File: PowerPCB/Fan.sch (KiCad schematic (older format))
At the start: 3 parts, among them Q2 Q_PMOS_DGS

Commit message: new relay added to PowerPCB, and its 3D model is added to the library
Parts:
- removed K?: FINDER-32.21-x300, Relay_THT:Relay_SPST_Finder_32.21-x300, symbol Relay:FINDER-32.21-x300
- added K3: ALFG2PF121, ALFG2PF121, symbol SamacSys_Parts:ALFG2PF121
- renumbered Q2 to Q1
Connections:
- wire segments 14 -> 15
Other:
- note added: "Relay: Panasonic ALFG2PF121 (Coil Voltage 12VDC, Coil Current 117mA, Contact Current Rating 31A)"
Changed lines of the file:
@@
 U 1 1 5E93960D
 P 1700 4450
-F 0 "R?" H 1770 4496 50  0000 L CNN
+F 0 "R8" H 1770 4496 50  0000 L CNN
 F 1 "100k" H 1770 4405 50  0000 L CNN
 F 2 "" V 1630 4450 50  0001 C CNN
@@
 VCC_12
 $Comp
-L Device:Q_PMOS_DGS Q2
+L Device:Q_PMOS_DGS Q1
 U 1 1 5EBA07C8
 P 3050 4650
-F 0 "Q?" H 3255 4696 50  0000 L CNN
+F 0 "Q1" H 3255 4696 50  0000 L CNN
 F 1 "Q_PMOS_DGS" H 3255 4605 50  0000 L CNN
 F 2 "" H 3250 4750 50  0001 C CNN
@@
 	3450 5150 3150 5150
 Wire Wire Line
-	4650 5000 4650 4850
-Wire Wire Line
-	5050 4950 5050 4850
+	6000 4500 5850 4500
 $Comp
-L power:GND #PWR?
+L power:GND #PWR01
 U 1 1 5EC359D9
-P 5050 4950
-F 0 "#PWR?" H 5050 4700 50  0001 C CNN
-F 1 "GND" H 5055 4777 50  0000 C CNN
-F 2 "" H 5050 4950 50  0001 C CNN
-F 3 "" H 5050 4950 50  0001 C CNN
-	1    5050 4950
+P 4450 4550
+F 0 "#PWR01" H 4450 4300 50  0001 C CNN
+F 1 "GND" H 4455 4377 50  0000 C CNN
+F 2 "" H 4450 4550 50  0001 C CNN
+F 3 "" H 4450 4550 50  0001 C CNN
+	1    4450 4550
+	1    0    0    -1
+$EndComp
+Text HLabel 4450 4400 0    50   Output ~ 0
+Fan-
+Text HLabel 6000 4500 2    50   Input ~ 0
+FanCtrl
+Text GLabel 6050 4400 2    50   Input ~ 0
+VCC_12
+Text Notes 5650 4950 0    50   ~ 0
+Relay: Panasonic ALFG2PF121 (Coil Voltage 12VDC, Coil Current 117mA, Contact Current Rating 31A)
+$Comp
+L SamacSys_Parts:ALFG2PF121 K3
+U 1 1 5ECACD05
+P 4650 4400
+F 0 "K3" H 5250 4665 50  0000 C CNN
+F 1 "ALFG2PF121" H 5250 4574 50  0000 C CNN
+F 2 "ALFG2PF121" H 5700 4500 50  0001 L CNN
+F 3 "http://www3.panasonic.biz/ac/e_download/control/relay/power/catalog/mech_eng_lfg.pdf" H 5700 4400 50  0001 L CNN
+F 4 "General Purpose Relays LF-G relay 1.8mm High cap type: 12V" H 5700 4300 50  0001 L CNN "Description"
+F 5 "23.3" H 5700 4200 50  0001 L CNN "Height"
+F 6 "Panasonic" H 5700 4100 50  0001 L CNN "Manufacturer_Name"
+F 7 "ALFG2PF121" H 5700 4000 50  0001 L CNN "Manufacturer_Part_Number"
+F 8 "769-ALFG2PF121" H 5700 3900 50  0001 L CNN "Mouser Part Number"
+F 9 "https://www.mouser.co.uk/ProductDetail/Panasonic-Industrial-Devices/ALFG2PF121?qs=WkdRfq4wf1O9EasQCWNl9Q%3D%3D" H 5700 3800 50  0001 L CNN "Mouser Price/Stock"
+F 10 "" H 5700 3700 50  0001 L CNN "RS Part Number"
+F 11 "" H 5700 3600 50  0001 L CNN "RS Price/Stock"
+	1    4650 4400
 	1    0    0    -1
 $EndComp
 Wire Wire Line
-	5150 4150 5150 4250
-$Comp
-L Relay:FINDER-32.21-x300 K?
-U 1 1 5EC302D7
-P 4850 4550
-F 0 "K?" H 5280 4596 50  0000 L CNN
-F 1 "FINDER-32.21-x300" H 5280 4505 50  0000 L CNN
-F 2 "Relay_THT:Relay_SPST_Finder_32.21-x300" H 6120 4520 50  0001 C CNN
-F 3 "http://gfinder.findernet.com/assets/Series/355/S32EN.pdf" H 4850 4550 50  0001 C CNN
-	1    4850 4550
-	1    0    0    -1
-$EndComp
-Text HLabel 5150 4150 1    50   Output ~ 0
-Fan-
-Text HLabel 4650 5000 3    50   Input ~ 0
-FanCtrl
-Text GLabel 4650 4150 1    50   Input ~ 0
-VCC_12
+	5850 4400 6050 4400
 Wire Wire Line
-	4650 4250 4650 4150
+	4450 4400 4650 4400
+Wire Wire Line
+	4650 4500 4450 4500
+Wire Wire Line
+	4450 4500 4450 4550
 $EndSCHEMATC

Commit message: Added footprints for all components
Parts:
- K3: footprint ALFG2PF121 -> SamacSys_Parts:ALFG2PF121
- Q1: footprint (none) -> Package_TO_SOT_SMD:SOT-323_SC-70_Handsoldering
- R8: footprint (none) -> Resistor_SMD:R_0805_2012Metric_Pad1.15x1.40mm_HandSolder
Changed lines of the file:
@@
 F 0 "R8" H 1770 4496 50  0000 L CNN
 F 1 "100k" H 1770 4405 50  0000 L CNN
-F 2 "" V 1630 4450 50  0001 C CNN
+F 2 "Resistor_SMD:R_0805_2012Metric_Pad1.15x1.40mm_HandSolder" V 1630 4450 50  0001 C CNN
 F 3 "~" H 1700 4450 50  0001 C CNN
 	1    1700 4450
@@
 F 0 "Q1" H 3255 4696 50  0000 L CNN
 F 1 "Q_PMOS_DGS" H 3255 4605 50  0000 L CNN
-F 2 "" H 3250 4750 50  0001 C CNN
+F 2 "Package_TO_SOT_SMD:SOT-323_SC-70_Handsoldering" H 3250 4750 50  0001 C CNN
 F 3 "~" H 3050 4650 50  0001 C CNN
 F 4 "X" H 3050 4650 50  0001 C CNN "Spice_Primitive"
@@
 F 0 "K3" H 5250 4665 50  0000 C CNN
 F 1 "ALFG2PF121" H 5250 4574 50  0000 C CNN
-F 2 "ALFG2PF121" H 5700 4500 50  0001 L CNN
+F 2 "SamacSys_Parts:ALFG2PF121" H 5700 4500 50  0001 L CNN
 F 3 "http://www3.panasonic.biz/ac/e_download/control/relay/power/catalog/mech_eng_lfg.pdf" H 5700 4400 50  0001 L CNN
 F 4 "General Purpose Relays LF-G relay 1.8mm High cap type: 12V" H 5700 4300 50  0001 L CNN "Description"

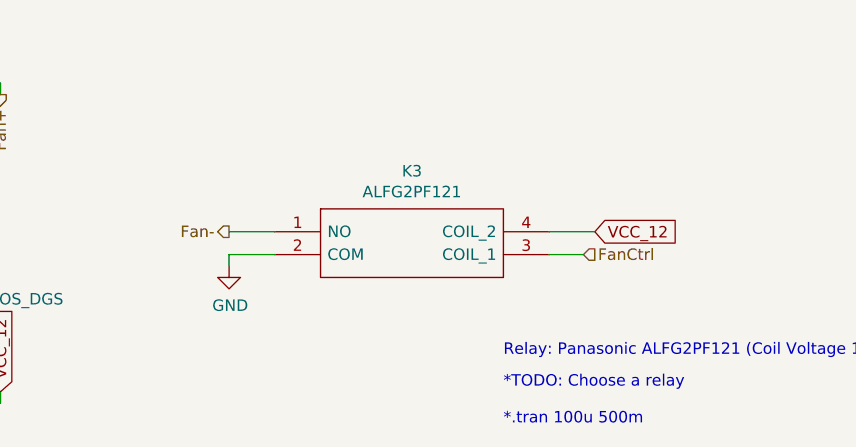
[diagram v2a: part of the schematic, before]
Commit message: Added 3A SPST relays for all relays
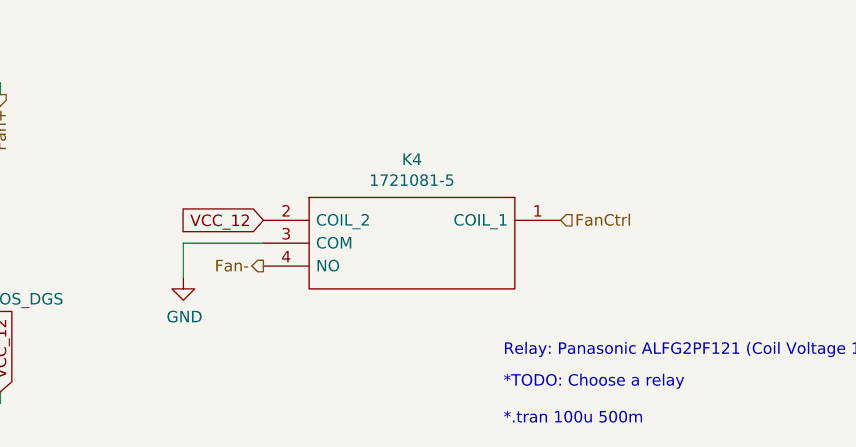
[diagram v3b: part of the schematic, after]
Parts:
- removed K3: ALFG2PF121, SamacSys_Parts:ALFG2PF121, symbol SamacSys_Parts:ALFG2PF121
- added K4: 1721081-5, SamacSys_Parts:17210815, symbol SamacSys_Parts:1721081-5
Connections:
- net Fan-: now also K4.4 (NO)
- net FanCtrl: now also K4.1 (COIL_1)
- net GND: now also K4.3 (COM)
- net VCC_12: now also K4.2 (COIL_2)
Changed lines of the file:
@@
 Wire Wire Line
 	3450 5150 3150 5150
-Wire Wire Line
-	6000 4500 5850 4500
-$Comp
-L power:GND #PWR01
-U 1 1 5EC359D9
-P 4450 4550
-F 0 "#PWR01" H 4450 4300 50  0001 C CNN
-F 1 "GND" H 4455 4377 50  0000 C CNN
-F 2 "" H 4450 4550 50  0001 C CNN
-F 3 "" H 4450 4550 50  0001 C CNN
-	1    4450 4550
-	1    0    0    -1
-$EndComp
-Text HLabel 4450 4400 0    50   Output ~ 0
-Fan-
-Text HLabel 6000 4500 2    50   Input ~ 0
-FanCtrl
-Text GLabel 6050 4400 2    50   Input ~ 0
-VCC_12
 Text Notes 5650 4950 0    50   ~ 0
 Relay: Panasonic ALFG2PF121 (Coil Voltage 12VDC, Coil Current 117mA, Contact Current Rating 31A)
 $Comp
-L SamacSys_Parts:ALFG2PF121 K3
-U 1 1 5ECACD05
-P 4650 4400
-F 0 "K3" H 5250 4665 50  0000 C CNN
-F 1 "ALFG2PF121" H 5250 4574 50  0000 C CNN
-F 2 "SamacSys_Parts:ALFG2PF121" H 5700 4500 50  0001 L CNN
-F 3 "http://www3.panasonic.biz/ac/e_download/control/relay/power/catalog/mech_eng_lfg.pdf" H 5700 4400 50  0001 L CNN
-F 4 "General Purpose Relays LF-G relay 1.8mm High cap type: 12V" H 5700 4300 50  0001 L CNN "Description"
-F 5 "23.3" H 5700 4200 50  0001 L CNN "Height"
-F 6 "Panasonic" H 5700 4100 50  0001 L CNN "Manufacturer_Name"
-F 7 "ALFG2PF121" H 5700 4000 50  0001 L CNN "Manufacturer_Part_Number"
-F 8 "769-ALFG2PF121" H 5700 3900 50  0001 L CNN "Mouser Part Number"
-F 9 "https://www.mouser.co.uk/ProductDetail/Panasonic-Industrial-Devices/ALFG2PF121?qs=WkdRfq4wf1O9EasQCWNl9Q%3D%3D" H 5700 3800 50  0001 L CNN "Mouser Price/Stock"
-F 10 "" H 5700 3700 50  0001 L CNN "RS Part Number"
-F 11 "" H 5700 3600 50  0001 L CNN "RS Price/Stock"
-	1    4650 4400
+L SamacSys_Parts:1721081-5 K4
+U 1 1 5ED203B8
+P 4600 4350
+F 0 "K4" H 5250 4615 50  0000 C CNN
+F 1 "1721081-5" H 5250 4524 50  0000 C CNN
+F 2 "SamacSys_Parts:17210815" H 5750 4450 50  0001 L CNN
+F 3 "https://www.te.com/commerce/DocumentDelivery/DDEController?Action=showdoc&DocId=Customer+Drawing%7F1721081%7FD1%7Fpdf%7FEnglish%7FENG_CD_1721081_D1.pdf%7F1721081-5" H 5750 4350 50  0001 L CNN
+F 4 "SPDT-NO PCB Mount Latching Relay Through Hole, 3 A, 12V dc" H 5750 4250 50  0001 L CNN "Description"
+F 5 "15" H 5750 4150 50  0001 L CNN "Height"
+F 6 "655-1721081-5" H 5750 4050 50  0001 L CNN "Mouser Part Number"
+F 7 "https://www.mouser.co.uk/ProductDetail/TE-Connectivity-OEG/1721081-5?qs=BqFpTYCQ3dI5UJqEVQS1jg%3D%3D" H 5750 3950 50  0001 L CNN "Mouser Price/Stock"
+F 8 "TE Connectivity" H 5750 3850 50  0001 L CNN "Manufacturer_Name"
+F 9 "1721081-5" H 5750 3750 50  0001 L CNN "Manufacturer_Part_Number"
+	1    4600 4350
+	1    0    0    -1
+$EndComp
+Text HLabel 5900 4350 2    50   Input ~ 0
+FanCtrl
+Text GLabel 4600 4350 0    50   Input ~ 0
+VCC_12
+Text HLabel 4600 4550 0    50   Output ~ 0
+Fan-
+$Comp
+L power:GND #PWR01
+U 1 1 5ED21FDC
+P 4250 4600
+F 0 "#PWR01" H 4250 4350 50  0001 C CNN
+F 1 "GND" H 4255 4427 50  0000 C CNN
+F 2 "" H 4250 4600 50  0001 C CNN
+F 3 "" H 4250 4600 50  0001 C CNN
+	1    4250 4600
 	1    0    0    -1
 $EndComp
 Wire Wire Line
-	5850 4400 6050 4400
+	4250 4600 4250 4450
 Wire Wire Line
-	4450 4400 4650 4400
-Wire Wire Line
-	4650 4500 4450 4500
-Wire Wire Line
-	4450 4500 4450 4550
+	4250 4450 4600 4450
 $EndSCHEMATC

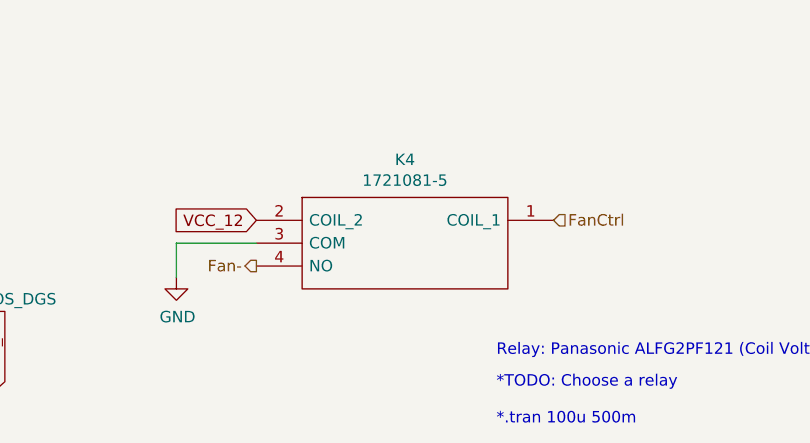
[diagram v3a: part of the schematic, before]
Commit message: Removed SPDT chassis mount relay, added diode footprint
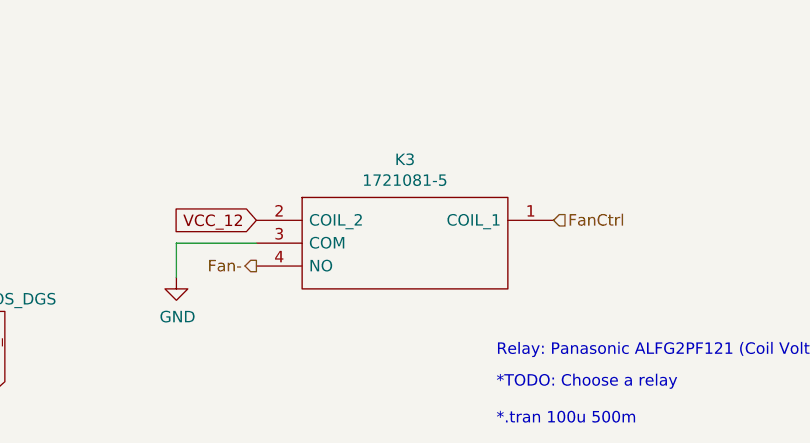
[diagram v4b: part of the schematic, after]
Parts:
- removed K4: 1721081-5, SamacSys_Parts:17210815, symbol SamacSys_Parts:1721081-5
- added K3: 1721081-5, SamacSys_Parts:17210815, symbol SamacSys_Parts:1721081-5
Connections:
- net Fan-: now also K3.4 (NO)
- net FanCtrl: now also K3.1 (COIL_1)
- net GND: now also K3.3 (COM)
- net VCC_12: now also K3.2 (COIL_2)
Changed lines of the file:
@@
 Text Notes 5650 4950 0    50   ~ 0
 Relay: Panasonic ALFG2PF121 (Coil Voltage 12VDC, Coil Current 117mA, Contact Current Rating 31A)
-$Comp
-L SamacSys_Parts:1721081-5 K4
-U 1 1 5ED203B8
-P 4600 4350
-F 0 "K4" H 5250 4615 50  0000 C CNN
-F 1 "1721081-5" H 5250 4524 50  0000 C CNN
-F 2 "SamacSys_Parts:17210815" H 5750 4450 50  0001 L CNN
-F 3 "https://www.te.com/commerce/DocumentDelivery/DDEController?Action=showdoc&DocId=Customer+Drawing%7F1721081%7FD1%7Fpdf%7FEnglish%7FENG_CD_1721081_D1.pdf%7F1721081-5" H 5750 4350 50  0001 L CNN
-F 4 "SPDT-NO PCB Mount Latching Relay Through Hole, 3 A, 12V dc" H 5750 4250 50  0001 L CNN "Description"
-F 5 "15" H 5750 4150 50  0001 L CNN "Height"
-F 6 "655-1721081-5" H 5750 4050 50  0001 L CNN "Mouser Part Number"
-F 7 "https://www.mouser.co.uk/ProductDetail/TE-Connectivity-OEG/1721081-5?qs=BqFpTYCQ3dI5UJqEVQS1jg%3D%3D" H 5750 3950 50  0001 L CNN "Mouser Price/Stock"
-F 8 "TE Connectivity" H 5750 3850 50  0001 L CNN "Manufacturer_Name"
-F 9 "1721081-5" H 5750 3750 50  0001 L CNN "Manufacturer_Part_Number"
-	1    4600 4350
-	1    0    0    -1
-$EndComp
 Text HLabel 5900 4350 2    50   Input ~ 0
 FanCtrl
@@
 Wire Wire Line
 	4250 4450 4600 4450
+$Comp
+L SamacSys_Parts:1721081-5 K3
+U 1 1 5ED4D566
+P 4600 4350
+F 0 "K3" H 5250 4615 50  0000 C CNN
+F 1 "1721081-5" H 5250 4524 50  0000 C CNN
+F 2 "SamacSys_Parts:17210815" H 5750 4450 50  0001 L CNN
+F 3 "https://www.te.com/commerce/DocumentDelivery/DDEController?Action=showdoc&DocId=Customer+Drawing%7F1721081%7FD1%7Fpdf%7FEnglish%7FENG_CD_1721081_D1.pdf%7F1721081-5" H 5750 4350 50  0001 L CNN
+F 4 "SPDT-NO PCB Mount Latching Relay Through Hole, 3 A, 12V dc" H 5750 4250 50  0001 L CNN "Description"
+F 5 "15" H 5750 4150 50  0001 L CNN "Height"
+F 6 "655-1721081-5" H 5750 4050 50  0001 L CNN "Mouser Part Number"
+F 7 "https://www.mouser.co.uk/ProductDetail/TE-Connectivity-OEG/1721081-5?qs=BqFpTYCQ3dI5UJqEVQS1jg%3D%3D" H 5750 3950 50  0001 L CNN "Mouser Price/Stock"
+F 8 "TE Connectivity" H 5750 3850 50  0001 L CNN "Manufacturer_Name"
+F 9 "1721081-5" H 5750 3750 50  0001 L CNN "Manufacturer_Part_Number"
+	1    4600 4350
+	1    0    0    -1
+$EndComp
 $EndSCHEMATC

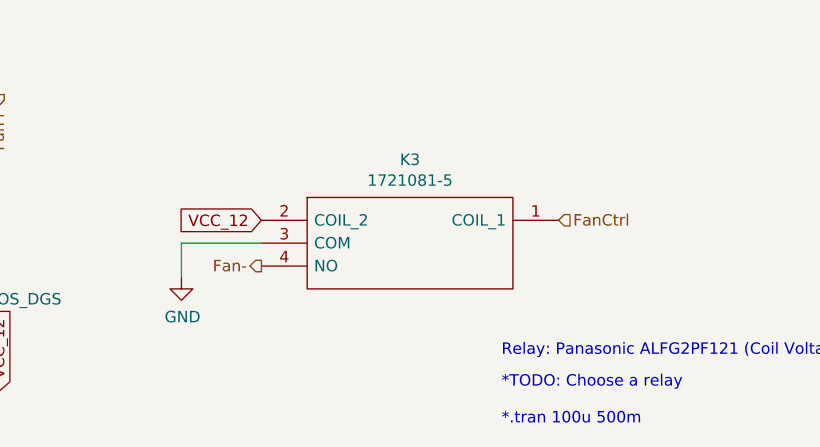
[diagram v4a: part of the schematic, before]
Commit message: Added Charge and Discharge relays
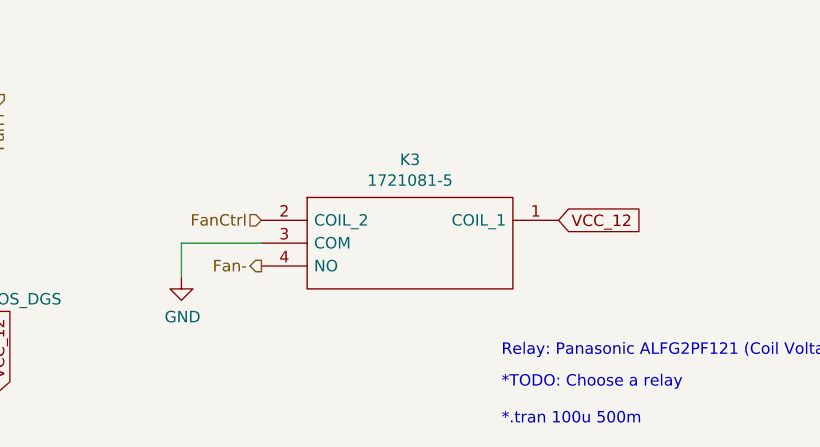
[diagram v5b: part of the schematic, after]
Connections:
- net FanCtrl: now also K3.2 (COIL_2); no longer K3.1 (COIL_1)
- net VCC_12: now also K3.1 (COIL_1); no longer K3.2 (COIL_2)
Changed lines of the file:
@@
 Text Notes 5650 4950 0    50   ~ 0
 Relay: Panasonic ALFG2PF121 (Coil Voltage 12VDC, Coil Current 117mA, Contact Current Rating 31A)
-Text HLabel 5900 4350 2    50   Input ~ 0
+Text HLabel 4600 4350 0    50   Input ~ 0
 FanCtrl
-Text GLabel 4600 4350 0    50   Input ~ 0
+Text GLabel 5900 4350 2    50   Input ~ 0
 VCC_12
 Text HLabel 4600 4550 0    50   Output ~ 0

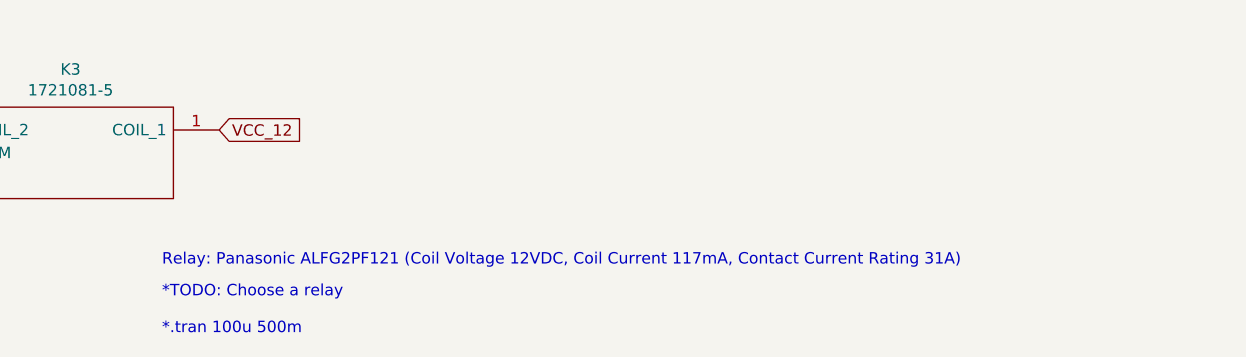
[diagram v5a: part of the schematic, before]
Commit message: Cleaned up main schematic and corrected text for fan relay
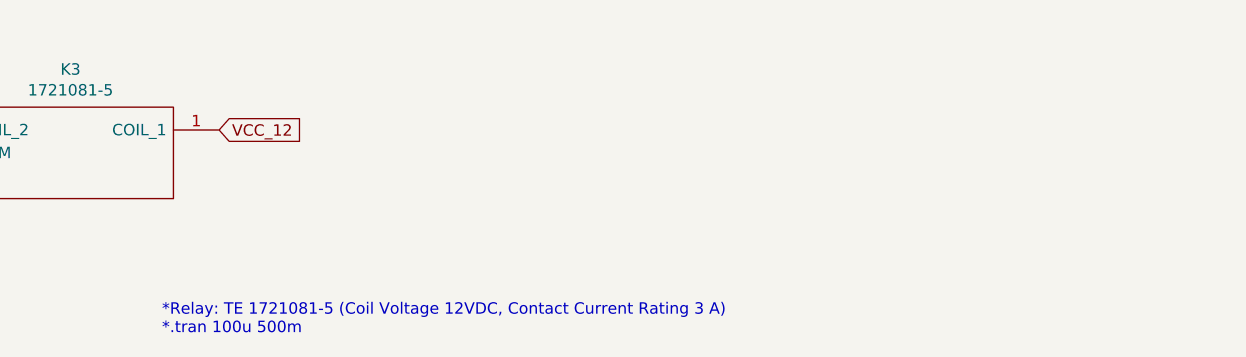
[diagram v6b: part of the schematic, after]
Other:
- note added: "*Relay: TE 1721081-5 (Coil Voltage 12VDC, Contact Current Rating 3 A)\n*.tran 100u 500m"
- note removed: "*TODO: Choose a relay\n\n*.tran 100u 500m"
- note removed: "Relay: Panasonic ALFG2PF121 (Coil Voltage 12VDC, Coil Current 117mA, Contact Current Rating 31A)"
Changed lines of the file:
@@
 	1550 4650 1700 4650
 Text Notes 5650 5250 0    50   ~ 0
-*TODO: Choose a relay\n\n*.tran 100u 500m
+*Relay: TE 1721081-5 (Coil Voltage 12VDC, Contact Current Rating 3 A)\n*.tran 100u 500m
 $Comp
 L Device:R R8
@@
 Wire Wire Line
 	3450 5150 3150 5150
-Text Notes 5650 4950 0    50   ~ 0
-Relay: Panasonic ALFG2PF121 (Coil Voltage 12VDC, Coil Current 117mA, Contact Current Rating 31A)
 Text HLabel 4600 4350 0    50   Input ~ 0
 FanCtrl

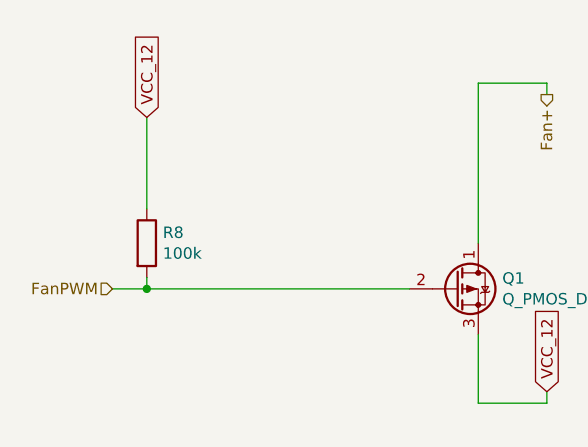
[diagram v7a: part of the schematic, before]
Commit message: Added bypass capacitors to CAN transceivers
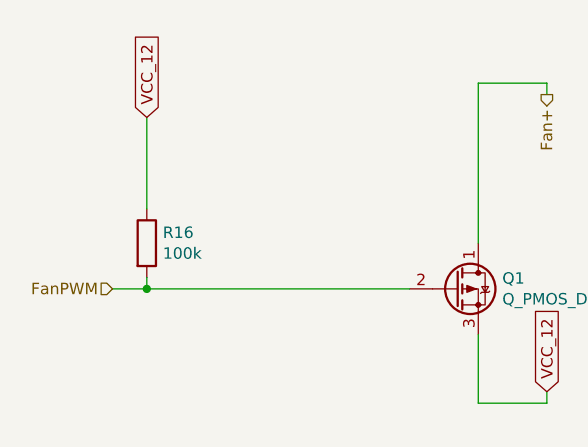
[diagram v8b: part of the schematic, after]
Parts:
- renumbered R8 to R16
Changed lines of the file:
@@
 *Relay: TE 1721081-5 (Coil Voltage 12VDC, Contact Current Rating 3 A)\n*.tran 100u 500m
 $Comp
-L Device:R R8
+L Device:R R16
 U 1 1 5E93960D
 P 1700 4450
-F 0 "R8" H 1770 4496 50  0000 L CNN
+F 0 "R16" H 1770 4496 50  0000 L CNN
 F 1 "100k" H 1770 4405 50  0000 L CNN
 F 2 "Resistor_SMD:R_0805_2012Metric_Pad1.15x1.40mm_HandSolder" V 1630 4450 50  0001 C CNN
@@
 Fan-
 $Comp
-L power:GND #PWR01
+L power:GND #PWR027
 U 1 1 5ED21FDC
 P 4250 4600
-F 0 "#PWR01" H 4250 4350 50  0001 C CNN
+F 0 "#PWR027" H 4250 4350 50  0001 C CNN
 F 1 "GND" H 4255 4427 50  0000 C CNN
 F 2 "" H 4250 4600 50  0001 C CNN
